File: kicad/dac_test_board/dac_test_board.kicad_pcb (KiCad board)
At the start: 2 copper layers, 54.1 x 50 mm, 43 parts, among them J1 Power, J2 Vcca_select, J3 In_Hi, J4 In_Lo, J5 Out_Hi, J6 Out_Lo, J7 Vccb_select, J9 Signals, U1 MCP4725A2T-E/CH, U2 SN74LVC8T245

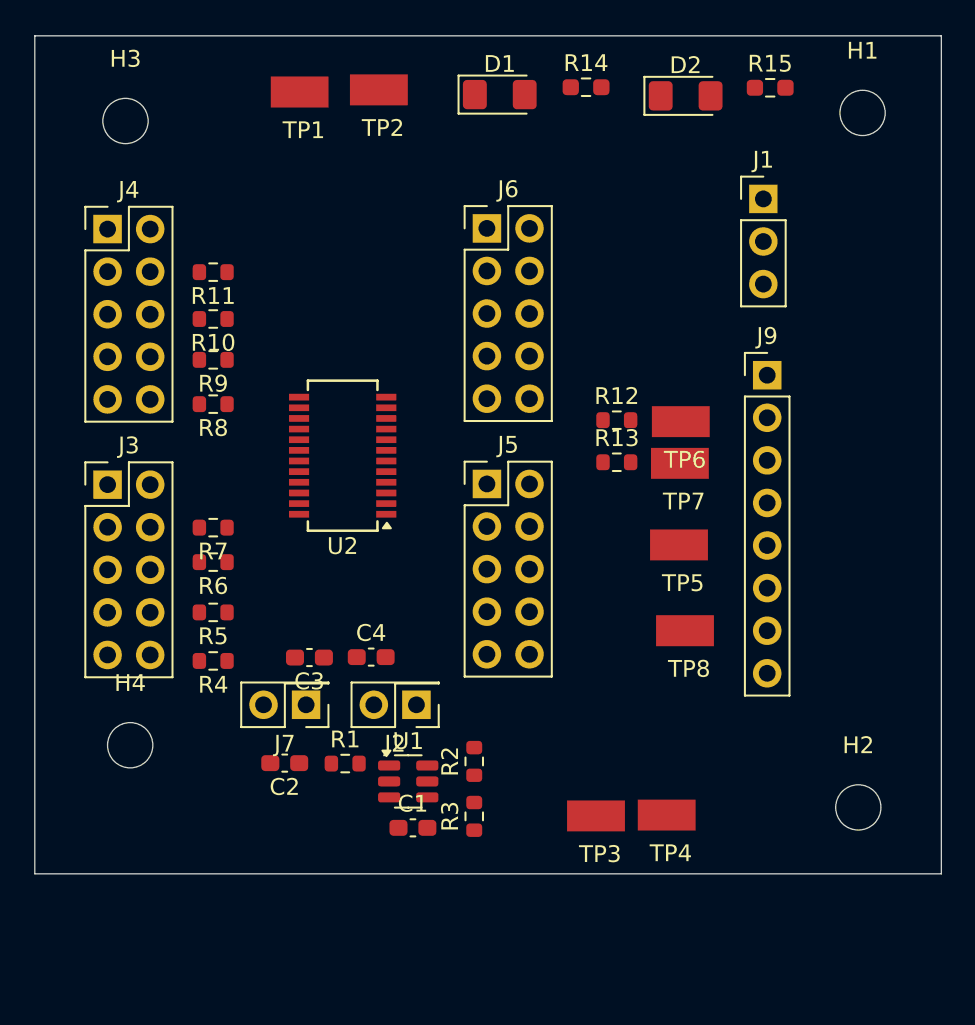
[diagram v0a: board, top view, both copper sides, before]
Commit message: changed In pinout to put GND in middle and added stemma qt
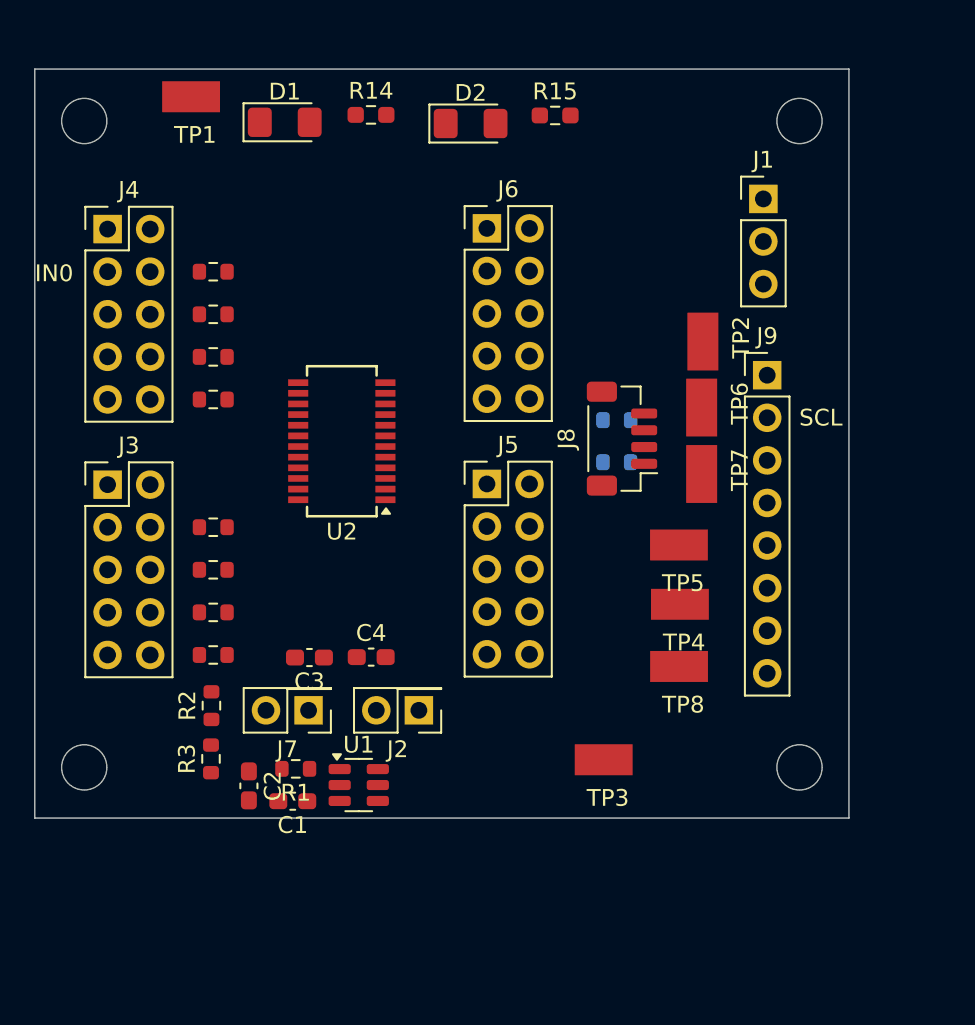
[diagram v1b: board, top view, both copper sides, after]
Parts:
- added J8: JST_SH_BM04B-SRSS-TB, Connector_JST:JST_SH_BM04B-SRSS-TB_1x04-1MP_P1.00mm_Vertical, F.Cu at (176.7, 97.5)
- R12, R13: moved to B.Cu
- moved TP2 24.5 mm to (181.6, 91.7), turned to 90 degrees
- moved R3 16.1 mm to (152.2, 116.6)
- moved R2 16.0 mm to (152.2, 113.4)
- moved D1 12.9 mm to (156.6, 78.6)
- moved D2 12.9 mm to (167.7, 78.7)
- moved R14 12.9 mm to (161.8, 78.2)
- moved R15 12.9 mm to (172.7, 78.2)
- moved TP4 12.6 mm to (180.2, 107.4)
- moved C1 7.34 mm to (157.1, 119.1), turned to 180 degrees
- moved TP1 6.48 mm to (151.0, 77.1)
- moved H2 4.24 mm to (187.3, 117.1)
- moved H1 3.79 mm to (187.3, 78.5)
- moved TP3 3.38 mm to (175.6, 116.6)
- moved H4 3.04 mm to (144.7, 117.1)
- moved R1 2.97 mm to (157.3, 117.2), turned to 180 degrees
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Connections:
- J3 pad 1: GND -> /IN04
- J3 pad 2: GND -> /IN04
- J3 pad 3: /IN04 -> /IN05
- J3 pad 4: /IN04 -> /IN05
- J3 pad 5: /IN05 -> GND
- J3 pad 6: /IN05 -> GND
- J4 pad 1: GND -> /IN00
- J4 pad 2: GND -> /IN00
- J4 pad 3: /IN00 -> /IN01
- J4 pad 4: /IN00 -> /IN01
- J4 pad 5: /IN01 -> GND
- J4 pad 6: /IN01 -> GND
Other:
- board size 54.1 x 50 mm -> 48.6 x 44.7 mm
- board text added: "IN0"
- board text added: "SCL"

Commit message: forgot the ldo... :(
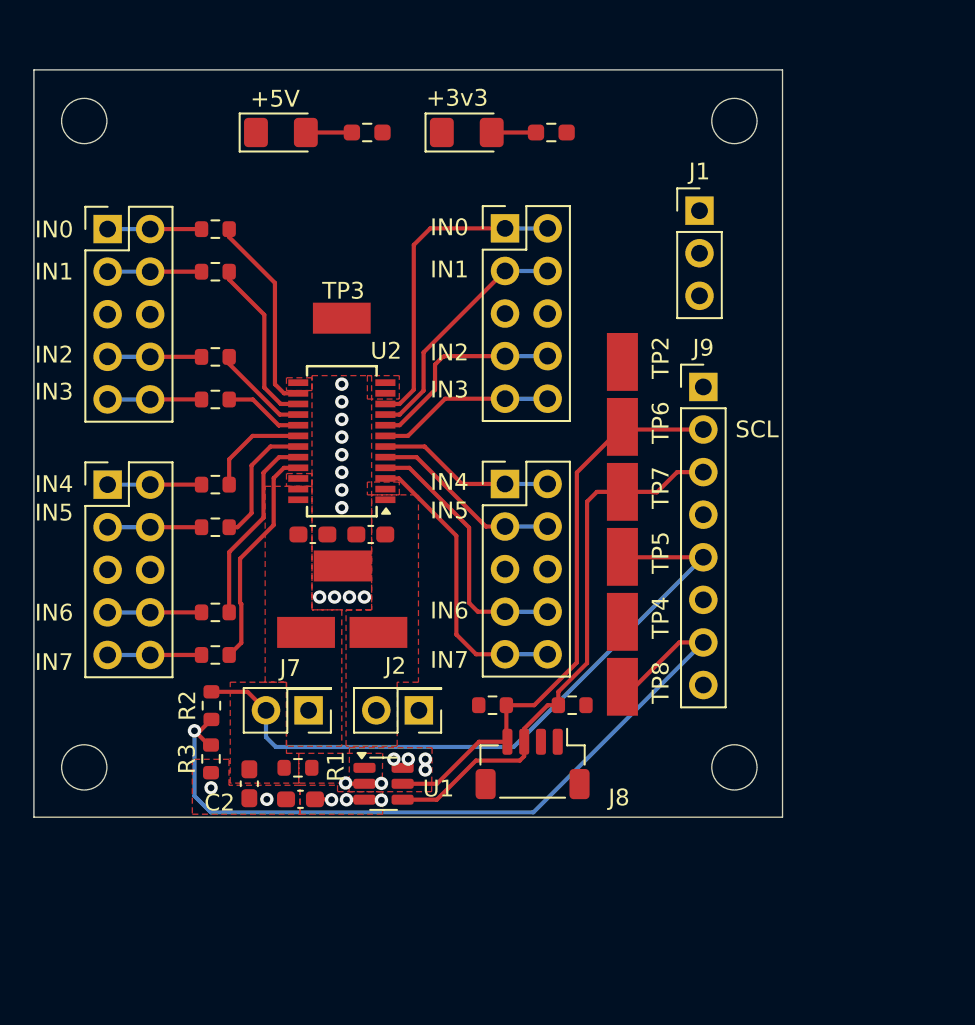
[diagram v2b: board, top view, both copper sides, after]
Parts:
- added TP10: TestPoint_Harwin, My Libraries:Harwin-S1751-46-Test-Point, F.Cu at (157.9, 109.0)
- added TP9: TestPoint_Harwin, My Libraries:Harwin-S1751-46-Test-Point, F.Cu at (162.2, 109.0)
- R12, R13: moved to F.Cu
- moved TP3 30.6 mm to (160.0, 90.3)
- moved TP1 29.4 mm to (160.1, 105.1), turned to 180 degrees
- moved J8 20.1 mm to (171.4, 116.9), turned to 180 degrees
- moved R12 18.5 mm to (169.0, 113.4)
- moved R13 14.7 mm to (173.8, 113.4), turned to 0 degrees
- moved C3 7.34 mm to (158.3, 103.2), turned to 0 degrees
- moved C4 7.32 mm to (161.7, 103.2), turned to 180 degrees
- moved TP2 4.95 mm to (176.8, 92.9)
- moved TP6 4.86 mm to (176.8, 96.8)
- moved TP7 4.84 mm to (176.8, 100.7)
- moved H1 3.88 mm to (183.4, 78.5)
- moved H2 3.88 mm to (183.4, 117.1)
- moved J1 3.87 mm to (181.4, 83.9)
- moved J9 3.87 mm to (181.6, 94.4)
- moved TP8 3.59 mm to (176.8, 112.3), turned to 90 degrees
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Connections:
- J5 pad 1: GND -> /BUF04
- J5 pad 2: GND -> /BUF04
- J5 pad 3: /BUF04 -> /BUF05
- J5 pad 4: /BUF04 -> /BUF05
- J5 pad 5: /BUF05 -> GND
- J5 pad 6: /BUF05 -> GND
- J6 pad 1: GND -> /BUF00
- J6 pad 2: GND -> /BUF00
- J6 pad 3: /BUF00 -> /BUF01
- J6 pad 4: /BUF00 -> /BUF01
- J6 pad 5: /BUF01 -> GND
- J6 pad 6: /BUF01 -> GND
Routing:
- net /Vdac_half: track 0.00 -> 47.4 mm, vias 0 -> 1
- net /Vdac_out: track 0.00 -> 41.2 mm
- net /I2C1_SCL: track 0.00 -> 34.8 mm
- net /I2C1_SDA: track 0.00 -> 33.1 mm
- net /BUF00: track 0.00 -> 19.1 mm
- net /BUF07: track 0.00 -> 17.5 mm
- net /BUF06: track 0.00 -> 15.9 mm
- net /BUF01: track 0.00 -> 14.6 mm
- net /B7: track 0.00 -> 13.4 mm
- net /BUF02: track 0.00 -> 12.3 mm
- net /B0: track 0.00 -> 12.0 mm
- net /B6: track 0.00 -> 11.6 mm
- net /BUF05: track 0.00 -> 11.4 mm
- net /BUF04: track 0.00 -> 10.6 mm
- net /BUF03: track 0.00 -> 10.6 mm
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- added copper zone on F.Cu, net +5V
- added copper zone on F.Cu, net /Vdac_out
- added copper zone on F.Cu, net GND
- added copper zone on In1.Cu, net GND
- added copper zone on F.Cu, net Net-(U1-VOUT)
- added copper zone on F.Cu, net Vcca
- added copper zone on F.Cu, net Vccb
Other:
- board size 48.6 x 44.7 mm -> 44.7 x 44.6 mm
- copper layers 2 -> 4
- rule pad_to_mask_clearance: 0 -> 0.0508
- board text added: "+3v3"
- board text added: "+5V"
- board text added: "IN1"
- board text added: "IN2"
- board text added: "IN3"
- board text added: "IN4"
- board text added: "IN5"
- board text added: "IN6"
- board text added: "IN7"

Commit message: initial rip-up for dac only
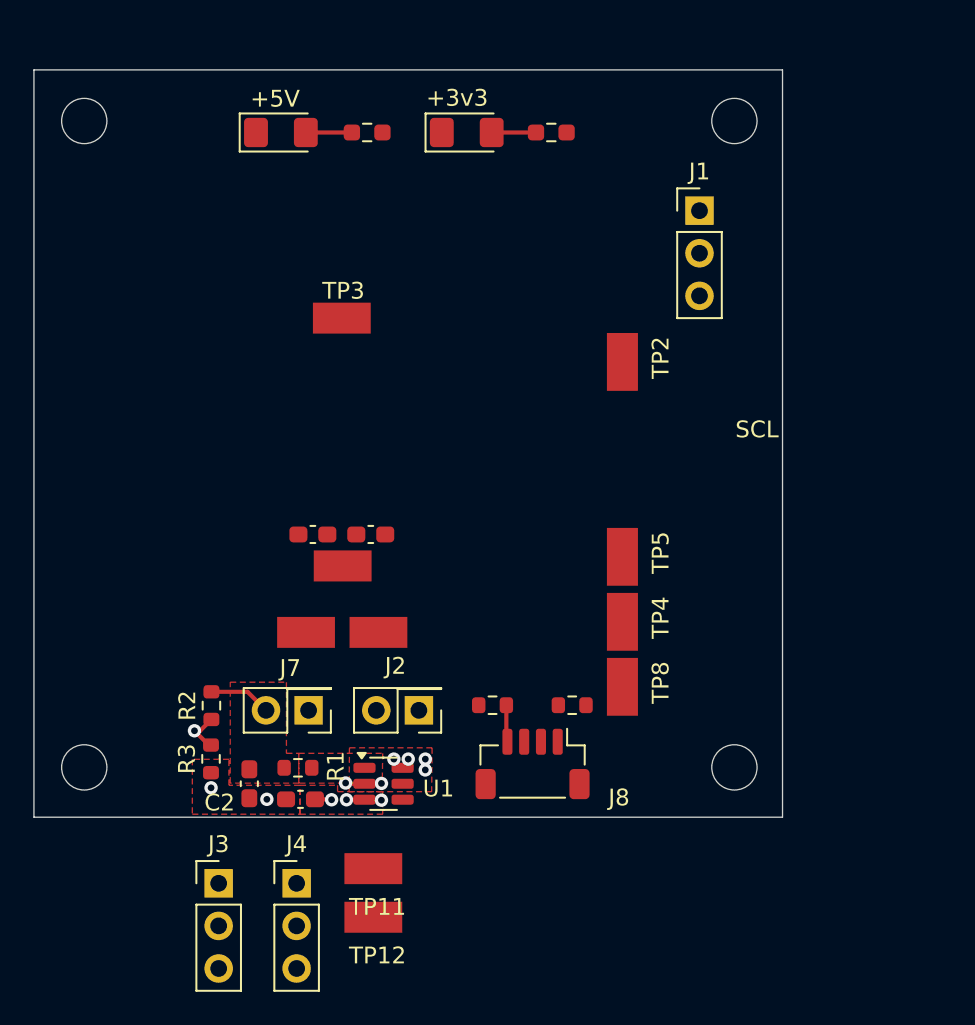
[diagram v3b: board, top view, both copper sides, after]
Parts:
- removed J5: Out_Hi, Connector_PinHeader_2.54mm:PinHeader_2x05_P2.54mm_Vertical
- removed J6: Out_Lo, Connector_PinHeader_2.54mm:PinHeader_2x05_P2.54mm_Vertical
- removed J9: Signals, Connector_PinHeader_2.54mm:PinHeader_1x08_P2.54mm_Vertical
- removed R10, R11, R4, R5, R6, R7, R8, R9: 220, Resistor_SMD:R_0603_1608Metric
- removed TP6, TP7: TestPoint_Harwin, My Libraries:Harwin-S1751-46-Test-Point
- removed U2: SN74LVC8T245, Package_SO:SSOP-24_3.9x8.7mm_P0.635mm
- added TP11: TestPoint_Harwin, My Libraries:Harwin-S1751-46-Test-Point, F.Cu at (161.9, 123.1)
- added TP12: TestPoint_Harwin, My Libraries:Harwin-S1751-46-Test-Point, F.Cu at (161.9, 126.0)
- J1: value Power -> Power_In
- J2: value Vcca_select -> Vcca_out
- J3: value In_Hi -> Power_Probe; footprint Connector_PinHeader_2.54mm:PinHeader_2x05_P2.54mm_Vertical -> Connector_PinHeader_2.54mm:PinHeader_1x03_P2.54mm_Vertical
- J4: value In_Lo -> I2C; footprint Connector_PinHeader_2.54mm:PinHeader_2x05_P2.54mm_Vertical -> Connector_PinHeader_2.54mm:PinHeader_1x03_P2.54mm_Vertical
- J7: value Vccb_select -> Vccb_out
- moved J4 40.6 mm to (157.3, 124.0)
- moved J3 24.7 mm to (152.7, 124.0)
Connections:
- J2 pad 1: +3V3 -> Vcca
- J2 pad 2: Vcca -> GND
- J3 pad 1: /IN04 -> +5V
- J3 pad 2: /IN04 -> GND
- J3 pad 3: /IN05 -> +3V3
- J4 pad 1: /IN00 -> /I2C1_SCL
- J4 pad 2: /IN00 -> GND
- J4 pad 3: /IN01 -> /I2C1_SDA
- J7 pad 2: /Vdac_out -> GND
- TP8 pad 1: /Vdac_half -> unconnected-(TP8-Pad1)
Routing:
- net /Vdac_half: track 47.4 -> 2.66 mm
- net /Vdac_out: track 41.2 -> 3.71 mm
- net /I2C1_SDA: track 33.1 -> 0.00 mm
- net /I2C1_SCL: track 34.8 -> 2.21 mm
- net /BUF00: track 19.1 -> 0.00 mm
- net /BUF07: track 17.5 -> 0.00 mm
- net /BUF06: track 15.9 -> 0.00 mm
- net /BUF01: track 14.6 -> 0.00 mm
- net /B7: track 13.4 -> 0.00 mm
- net /BUF02: track 12.3 -> 0.00 mm
- net /B0: track 12.0 -> 0.00 mm
- net /B6: track 11.6 -> 0.00 mm
- net /BUF05: track 11.4 -> 0.00 mm
- net /BUF04: track 10.6 -> 0.00 mm
- net /BUF03: track 10.6 -> 0.00 mm
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- removed copper zone on F.Cu, net Vcca
- removed copper zone on F.Cu, net Vccb
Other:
- board text removed: "IN0"
- board text removed: "IN1"
- board text removed: "IN2"
- board text removed: "IN3"
- board text removed: "IN4"
- board text removed: "IN5"
- board text removed: "IN6"
- board text removed: "IN7"

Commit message: pcb passes drc
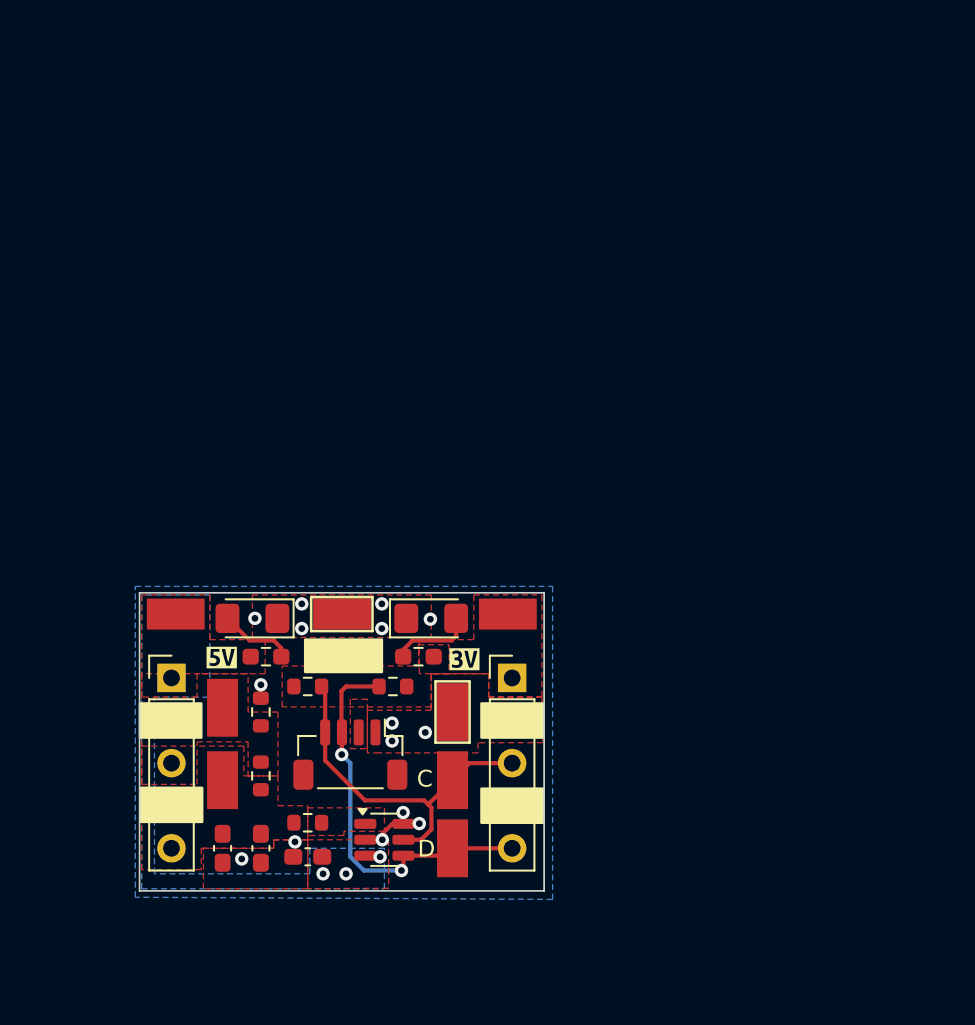
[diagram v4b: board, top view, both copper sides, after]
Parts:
- removed C3: 1u, Capacitor_SMD:C_0603_1608Metric_Pad1.08x0.95mm_HandSolder
- removed H1, H2, H3, H4: MountingHole, MountingHole:MountingHole_2.7mm
- removed J1: Power_In, Connector_PinHeader_2.54mm:PinHeader_1x03_P2.54mm_Vertical
- removed J3: Power_Probe, Connector_PinHeader_2.54mm:PinHeader_1x03_P2.54mm_Vertical
- removed J7: Vccb_out, Connector_PinHeader_2.54mm:PinHeader_2x01_P2.54mm_Vertical
- removed TP1, TP10, TP3, TP9: TestPoint_Harwin, My Libraries:Harwin-S1751-46-Test-Point
- added TP6: TestPoint_Harwin, My Libraries:Harwin-S1751-46-Test-Point, F.Cu at (150.1, 108.0)
- added TP7: TestPoint_Harwin, My Libraries:Harwin-S1751-46-Test-Point, F.Cu at (169.9, 108.0)
- added kibuzzard-67311944: G***, kibuzzard-67311944, B.Cu at (155.1, 116.5)
- added kibuzzard-67311A27: G***, kibuzzard-67311A27, F.Cu at (152.9, 110.5)
- added kibuzzard-67311A33: G***, kibuzzard-67311A33, F.Cu at (167.3, 110.6)
- J2: value Vcca_out -> Vout; footprint Connector_PinHeader_2.54mm:PinHeader_2x01_P2.54mm_Vertical -> Connector_PinHeader_2.54mm:PinHeader_1x05_P2.54mm_Vertical
- J4: footprint Connector_PinHeader_2.54mm:PinHeader_1x03_P2.54mm_Vertical -> Connector_PinHeader_2.54mm:PinHeader_1x05_P2.54mm_Vertical
- moved R15 32.3 mm to (164.6, 110.5)
- moved R14 31.8 mm to (155.5, 110.5), turned to 0 degrees
- moved D2 29.1 mm to (165.4, 108.2)
- moved D1 29.0 mm to (154.7, 108.2), turned to 180 degrees
- moved TP5 27.3 mm to (152.9, 117.9)
- moved TP8 23.9 mm to (152.9, 113.5)
- moved TP2 23.2 mm to (166.6, 113.8), turned to -90 degrees
- moved C4 20.7 mm to (152.9, 121.9), turned to -90 degrees
- moved J4 17.8 mm to (170.2, 111.8)
- moved TP4 16.7 mm to (160.0, 108.0), turned to 180 degrees
- moved J2 14.9 mm to (149.9, 111.8), turned to 0 degrees
- moved R12 11.1 mm to (158.0, 112.3)
- moved J8 10.9 mm to (160.5, 116.3)
- moved R13 10.8 mm to (163.1, 112.3)
- moved TP11 7.08 mm to (166.6, 117.9), turned to 90 degrees
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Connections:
- C2 pad 1: /Vdac_out -> Vdac_out
- C4 pad 1: Vcca -> Vdac_out
- J2 pad 1: Vcca -> +5V
- J4 pad 1: /I2C1_SCL -> +3V3
- J4 pad 3: /I2C1_SDA -> /I2C1_SCL
- R1 pad 2: /Vdac_out -> Vdac_out
- R2 pad 2: /Vdac_out -> Vdac_out
- TP5 pad 1: /Vdac_out -> Vdac_out
- TP8 pad 1: unconnected-(TP8-Pad1) -> /Vdac_half
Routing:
- net /I2C1_SDA: track 0.00 -> 23.5 mm, vias 0 -> 2
- net /I2C1_SCL: track 2.21 -> 21.3 mm
- net /Vdac_out: track 3.71 -> 0.00 mm
- net /Vdac_half: track 2.66 -> 0.00 mm, vias 1 -> 0
- net GND: track 2.77 -> 5.31 mm, vias 8 -> 15
- net Net-(D2-A): track 2.64 -> 4.96 mm
- net +5V: track 3.10 -> 0.91 mm
- net Net-(D1-A): track 2.74 -> 4.46 mm
- added copper zone on F.Cu, net +3V3
- added copper zone on B.Cu, net +5V
- added copper zone on F.Cu, net /Vdac_half
- added copper zone on B.Cu, net GND
- added copper zone on F.Cu, net Vdac_out
- removed copper zone on F.Cu, net /Vdac_out
- removed copper zone on In1.Cu, net GND
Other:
- board size 44.7 x 44.6 mm -> 24.1 x 17.8 mm
- copper layers 4 -> 2
- board text added: "C"
- board text added: "D"
- board text removed: "+3v3"
- board text removed: "+5V"
- board text removed: "SCL"
